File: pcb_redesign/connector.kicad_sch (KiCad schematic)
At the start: 8 parts, among them IC1 SPX1117M3-L-3-3_TR, J2 USB_B

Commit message: finished design
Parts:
- removed J2: USB_B, micro_usb_type_b:AMPHENOL_10118192-0002LF, symbol Connector:USB_B
- added J1: USB_B_Micro, micro_usb_type_b:AMPHENOL_10118192-0002LF, symbol Connector:USB_B_Micro
- C4: footprint 1uF_cap_0603:CL10A105KB8NNNC -> Capacitor_SMD:C_0603_1608Metric
- IC1: footprint SOT230P700X180-4N -> 3.3v_reg:SOT230P700X180-4N
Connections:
- net 3.7_UNREG: now also R3.1, J1.1 (VBUS)
- net D+: now also J1.3 (D+)
- net D-: now also J1.2 (D-)
- net GND: now also J1.5 (GND), J1.S1 (in1), J1.S2 (in2), J1.S3 (in3), J1.S4 (in4), J1.S5 (in5), J1.S6 (in6)
- net VCC_3V3: no longer R3.1
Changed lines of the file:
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@@
   (junction (at 177.8 35.56) (diameter 0) (color 0 0 0 0)
   )
+  (junction (at 35.56 95.25) (diameter 0) (color 0 0 0 0)
+  )
   (junction (at 177.8 54.61) (diameter 0) (color 0 0 0 0)
   )
@@
   (junction (at 57.15 54.61) (diameter 0) (color 0 0 0 0)
   )
+  (junction (at 35.56 100.33) (diameter 0) (color 0 0 0 0)
+  )
   (junction (at 232.41 55.88) (diameter 0) (color 0 0 0 0)
   )
+  (junction (at 35.56 102.87) (diameter 0) (color 0 0 0 0)
+  )
+  (junction (at 35.56 92.71) (diameter 0) (color 0 0 0 0)
+  )
+  (junction (at 57.15 80.01) (diameter 0) (color 0 0 0 0)
+  )
+  (junction (at 35.56 113.03) (diameter 0) (color 0 0 0 0)
+  )
   (junction (at 116.84 54.61) (diameter 0) (color 0 0 0 0)
   )
@@
   (junction (at 110.49 38.1) (diameter 0) (color 0 0 0 0)
   )
+  (junction (at 35.56 97.79) (diameter 0) (color 0 0 0 0)
+  )
   (junction (at 213.36 55.88) (diameter 0) (color 0 0 0 0)
   )
-  (no_connect (at 40.64 106.68))
-  (wire (pts (xy 78.74 80.01) (xy 80.01 80.01))
+  (no_connect (at 50.8 101.6))
+  (wire (pts (xy 57.15 80.01) (xy 80.01 80.01))
     (stroke (width 0) (type default))
   )
@@
     (stroke (width 0) (type default))
   )
+  (wire (pts (xy 35.56 102.87) (xy 35.56 113.03))
+    (stroke (width 0) (type default))
+  )
   (wire (pts (xy 50.8 99.06) (xy 142.24 99.06))
     (stroke (width 0) (type default))
@@
     (stroke (width 0) (type default))
   )
-  (wire (pts (xy 78.74 69.85) (xy 78.74 80.01))
-    (stroke (width 0) (type default))
-  )
   (wire (pts (xy 199.39 39.37) (xy 207.01 39.37))
     (stroke (width 0) (type default))
   )
-  (wire (pts (xy 57.15 91.44) (xy 57.15 54.61))
+  (wire (pts (xy 57.15 91.44) (xy 57.15 80.01))
     (stroke (width 0) (type default))
   )
@@
     (stroke (width 0) (type default))
   )
-  (wire (pts (xy 17.78 113.03) (xy 43.18 113.03))
+  (wire (pts (xy 17.78 113.03) (xy 35.56 113.03))
+    (stroke (width 0) (type default))
+  )
+  (wire (pts (xy 35.56 100.33) (xy 35.56 102.87))
     (stroke (width 0) (type default))
   )
@@
     (stroke (width 0) (type default))
   )
-  (wire (pts (xy 232.41 69.85) (xy 78.74 69.85))
-    (stroke (width 0) (type default))
-  )
   (wire (pts (xy 177.8 35.56) (xy 177.8 46.99))
     (stroke (width 0) (type default))
@@
     (stroke (width 0) (type default))
   )
+  (wire (pts (xy 35.56 113.03) (xy 43.18 113.03))
+    (stroke (width 0) (type default))
+  )
   (wire (pts (xy 182.88 46.99) (xy 177.8 46.99))
     (stroke (width 0) (type default))
@@
     (stroke (width 0) (type default))
   )
+  (wire (pts (xy 35.56 92.71) (xy 35.56 95.25))
+    (stroke (width 0) (type default))
+  )
   (wire (pts (xy 52.07 54.61) (xy 57.15 54.61))
     (stroke (width 0) (type default))
@@
     (stroke (width 0) (type default))
   )
+  (wire (pts (xy 57.15 80.01) (xy 57.15 54.61))
+    (stroke (width 0) (type default))
+  )
   (wire (pts (xy 116.84 41.91) (xy 116.84 38.1))
     (stroke (width 0) (type default))
@@
     (stroke (width 0) (type default))
   )
+  (wire (pts (xy 35.56 90.17) (xy 35.56 92.71))
+    (stroke (width 0) (type default))
+  )
   (wire (pts (xy 43.18 113.03) (xy 43.18 106.68))
     (stroke (width 0) (type default))
@@
     (stroke (width 0) (type default))
   )
+  (wire (pts (xy 35.56 95.25) (xy 35.56 97.79))
+    (stroke (width 0) (type default))
+  )
   (wire (pts (xy 50.8 91.44) (xy 57.15 91.44))
     (stroke (width 0) (type default))
@@
   )
   (wire (pts (xy 102.87 41.91) (xy 102.87 38.1))
+    (stroke (width 0) (type default))
+  )
+  (wire (pts (xy 35.56 97.79) (xy 35.56 100.33))
     (stroke (width 0) (type default))
   )
@@
       (effects (font (size 1.27 1.27)) (justify left))
     )
-    (property "Footprint" "1uF_cap_0603:CL10A105KB8NNNC" (at 102.87 48.26 0)
+    (property "Footprint" "Capacitor_SMD:C_0603_1608Metric" (at 102.87 48.26 0)
       (effects (font (size 1.27 1.27)) hide)
     )
@@
     )
   )
-  (symbol (lib_id "Connector:USB_B") (at 43.18 96.52 0) (unit 1)
-    (in_bom yes) (on_board yes) (dnp no) (fields_autoplaced)
-    (property "Reference" "J2" (at 43.18 85.09 0)
-      (effects (font (size 1.27 1.27)))
-    )
-    (property "Value" "USB_B" (at 43.18 87.63 0)
-      (effects (font (size 1.27 1.27)))
-    )
-    (property "Footprint" "micro_usb_type_b:AMPHENOL_10118192-0002LF" (at 46.99 97.79 0)
-      (effects (font (size 1.27 1.27)) hide)
-    )
-    (property "Datasheet" " ~" (at 46.99 97.79 0)
+  (symbol (lib_id "Connector:USB_B_Micro") (at 43.18 96.52 0) (unit 1)
+    (in_bom yes) (on_board yes) (dnp no) (fields_autoplaced)
+    (property "Reference" "J1" (at 43.18 85.09 0)
+      (effects (font (size 1.27 1.27)))
+    )
+    (property "Value" "USB_B_Micro" (at 43.18 87.63 0)
+      (effects (font (size 1.27 1.27)))
+    )
+    (property "Footprint" "micro_usb_type_b:AMPHENOL_10118192-0002LF" (at 48.26 106.68 0)
+      (effects (font (size 1.27 1.27)) hide)
+    )
+    (property "Datasheet" "~" (at 46.99 97.79 0)
       (effects (font (size 1.27 1.27)) hide)
     )
@@
     (pin "4")
     (pin "5")
-    (instances
-      (project "pcb_redesign"
-        (path "/fb030e39-7dd3-46a0-8379-c26b3ef1b0a0/2939bd35-2732-40e2-8b47-7f9c13890d54"
-          (reference "J2") (unit 1)
+    (pin "S5")
+    (pin "S6")
+    (pin "S1")
+    (pin "S2")
+    (pin "S3")
+    (pin "S4")
+    (instances
+      (project "pcb_redesign"
+        (path "/fb030e39-7dd3-46a0-8379-c26b3ef1b0a0/2939bd35-2732-40e2-8b47-7f9c13890d54"
+          (reference "J1") (unit 1)
         )
       )
@@
       (effects (font (size 1.27 1.27)))
     )
-    (property "Footprint" "SOT230P700X180-4N" (at 168.91 49.53 0)
+    (property "Footprint" "3.3v_reg:SOT230P700X180-4N" (at 168.91 49.53 0)
       (effects (font (size 1.27 1.27)) (justify left) hide)
     )

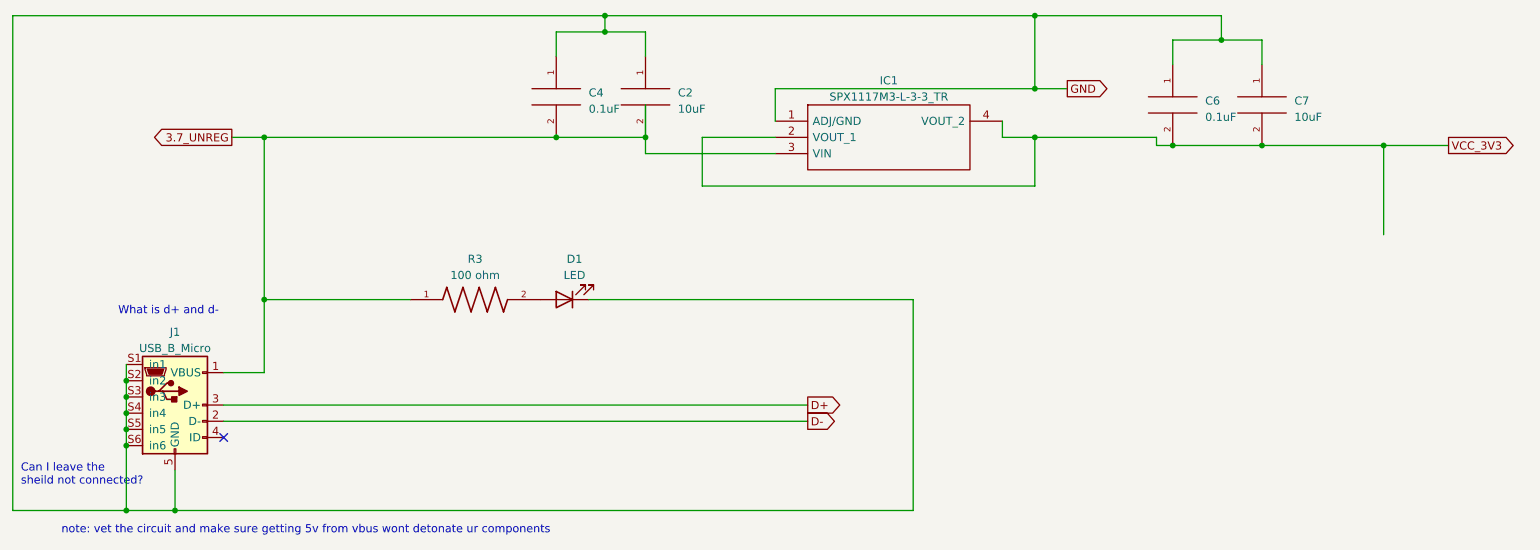
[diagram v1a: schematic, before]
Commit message: finished adding decoupling caps, shipped off to jlc
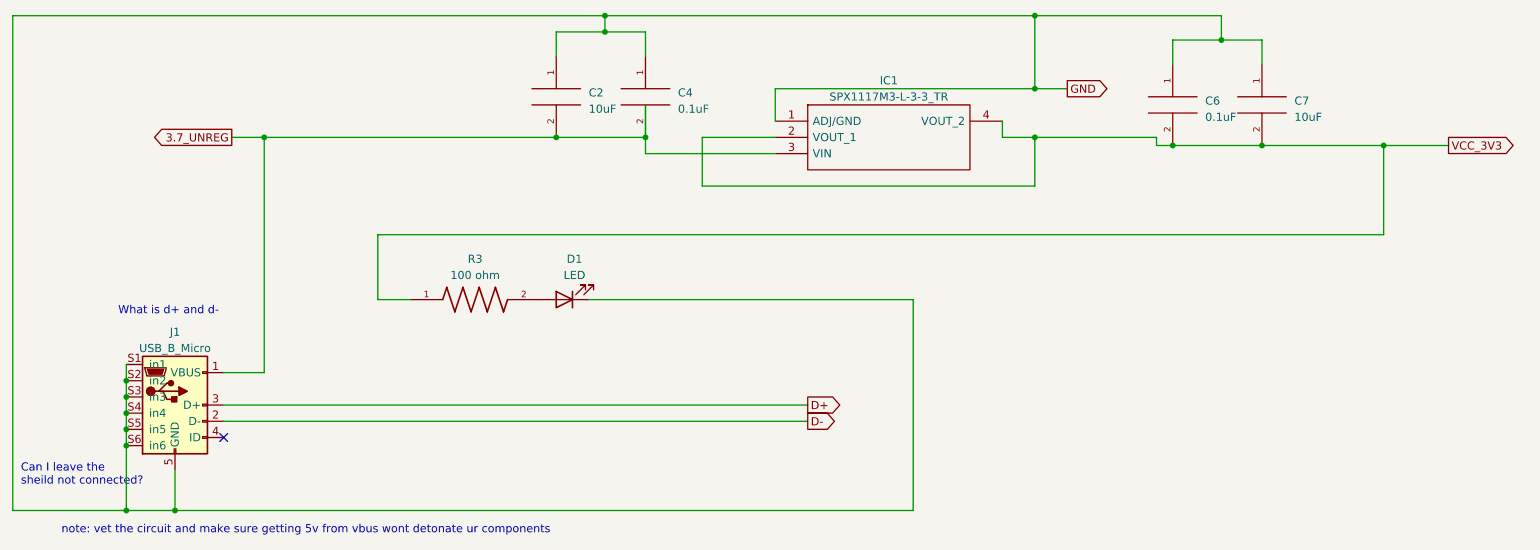
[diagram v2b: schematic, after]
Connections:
- net 3.7_UNREG: no longer R3.1
- net VCC_3V3: now also R3.1
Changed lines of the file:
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@@
 (kicad_sch (version 20230121) (generator eeschema)
   (paper "A4")
+  (junction (at 102.87 54.61) (diameter 0) (color 0 0 0 0)
+  )
   (junction (at 207.01 39.37) (diameter 0) (color 0 0 0 0)
   )
@@
   (junction (at 177.8 54.61) (diameter 0) (color 0 0 0 0)
   )
-  (junction (at 102.87 54.61) (diameter 0) (color 0 0 0 0)
-  )
   (junction (at 57.15 54.61) (diameter 0) (color 0 0 0 0)
   )
@@
   (junction (at 35.56 92.71) (diameter 0) (color 0 0 0 0)
   )
-  (junction (at 57.15 80.01) (diameter 0) (color 0 0 0 0)
-  )
   (junction (at 35.56 113.03) (diameter 0) (color 0 0 0 0)
   )
@@
   )
   (no_connect (at 50.8 101.6))
-  (wire (pts (xy 57.15 80.01) (xy 80.01 80.01))
-    (stroke (width 0) (type default))
-  )
   (wire (pts (xy 177.8 35.56) (xy 207.01 35.56))
     (stroke (width 0) (type default))
@@
     (stroke (width 0) (type default))
   )
+  (wire (pts (xy 74.93 80.01) (xy 74.93 69.85))
+    (stroke (width 0) (type default))
+  )
   (wire (pts (xy 199.39 43.18) (xy 199.39 39.37))
     (stroke (width 0) (type default))
@@
     (stroke (width 0) (type default))
   )
-  (wire (pts (xy 57.15 91.44) (xy 57.15 80.01))
-    (stroke (width 0) (type default))
-  )
   (wire (pts (xy 110.49 35.56) (xy 177.8 35.56))
     (stroke (width 0) (type default))
@@
     (stroke (width 0) (type default))
   )
+  (wire (pts (xy 74.93 69.85) (xy 232.41 69.85))
+    (stroke (width 0) (type default))
+  )
   (wire (pts (xy 35.56 100.33) (xy 35.56 102.87))
     (stroke (width 0) (type default))
   )
+  (wire (pts (xy 102.87 54.61) (xy 116.84 54.61))
+    (stroke (width 0) (type default))
+  )
   (wire (pts (xy 110.49 38.1) (xy 116.84 38.1))
     (stroke (width 0) (type default))
@@
     (stroke (width 0) (type default))
   )
-  (wire (pts (xy 57.15 80.01) (xy 57.15 54.61))
+  (wire (pts (xy 80.01 80.01) (xy 74.93 80.01))
+    (stroke (width 0) (type default))
+  )
+  (wire (pts (xy 57.15 54.61) (xy 57.15 91.44))
     (stroke (width 0) (type default))
   )
@@
   )
   (wire (pts (xy 196.85 55.88) (xy 199.39 55.88))
-    (stroke (width 0) (type default))
-  )
-  (wire (pts (xy 102.87 54.61) (xy 116.84 54.61))
     (stroke (width 0) (type default))
   )
@@
     )
   )
-  (symbol (lib_id "pspice:C") (at 102.87 48.26 0) (unit 1)
-    (in_bom yes) (on_board yes) (dnp no) (fields_autoplaced)
-    (property "Reference" "C4" (at 107.95 47.625 0)
-      (effects (font (size 1.27 1.27)) (justify left))
-    )
-    (property "Value" "0.1uF" (at 107.95 50.165 0)
-      (effects (font (size 1.27 1.27)) (justify left))
-    )
-    (property "Footprint" "Capacitor_SMD:C_0603_1608Metric" (at 102.87 48.26 0)
-      (effects (font (size 1.27 1.27)) hide)
-    )
-    (property "Datasheet" "~" (at 102.87 48.26 0)
-      (effects (font (size 1.27 1.27)) hide)
-    )
-    (pin "1")
-    (pin "2")
-    (instances
-      (project "pcb_redesign"
-        (path "/fb030e39-7dd3-46a0-8379-c26b3ef1b0a0/2939bd35-2732-40e2-8b47-7f9c13890d54"
-          (reference "C4") (unit 1)
-        )
-      )
-    )
-  )
   (symbol (lib_id "pspice:C") (at 213.36 49.53 0) (unit 1)
     (in_bom yes) (on_board yes) (dnp no) (fields_autoplaced)
@@
         (path "/fb030e39-7dd3-46a0-8379-c26b3ef1b0a0/2939bd35-2732-40e2-8b47-7f9c13890d54"
           (reference "C7") (unit 1)
-        )
-      )
-    )
-  )
-  (symbol (lib_id "pspice:C") (at 116.84 48.26 0) (unit 1)
-    (in_bom yes) (on_board yes) (dnp no) (fields_autoplaced)
-    (property "Reference" "C2" (at 121.92 47.625 0)
-      (effects (font (size 1.27 1.27)) (justify left))
-    )
-    (property "Value" "10uF" (at 121.92 50.165 0)
-      (effects (font (size 1.27 1.27)) (justify left))
-    )
-    (property "Footprint" "10uF_cap_0603:CAPC1608X90N" (at 116.84 48.26 0)
-      (effects (font (size 1.27 1.27)) hide)
-    )
-    (property "Datasheet" "~" (at 116.84 48.26 0)
-      (effects (font (size 1.27 1.27)) hide)
-    )
-    (pin "1")
-    (pin "2")
-    (instances
-      (project "pcb_redesign"
-        (path "/fb030e39-7dd3-46a0-8379-c26b3ef1b0a0/2939bd35-2732-40e2-8b47-7f9c13890d54"
-          (reference "C2") (unit 1)
         )
       )
@@
     (pin "4")
     (pin "5")
-    (pin "S5")
-    (pin "S6")
     (pin "S1")
     (pin "S2")
     (pin "S3")
     (pin "S4")
+    (pin "S5")
+    (pin "S6")
     (instances
       (project "pcb_redesign"
@@
         )
       )
+    )
+  )
+  (symbol (lib_id "pspice:C") (at 102.87 48.26 0) (unit 1)
+    (in_bom yes) (on_board yes) (dnp no) (fields_autoplaced)
+    (property "Reference" "C2" (at 107.95 47.625 0)
+      (effects (font (size 1.27 1.27)) (justify left))
+    )
+    (property "Value" "10uF" (at 107.95 50.165 0)
+      (effects (font (size 1.27 1.27)) (justify left))
+    )
+    (property "Footprint" "10uF_cap_0603:CAPC1608X90N" (at 102.87 48.26 0)
+      (effects (font (size 1.27 1.27)) hide)
+    )
+    (property "Datasheet" "~" (at 102.87 48.26 0)
+      (effects (font (size 1.27 1.27)) hide)
+    )
+    (pin "1")
+    (pin "2")
+    (instances
+      (project "pcb_redesign"
+        (path "/fb030e39-7dd3-46a0-8379-c26b3ef1b0a0/2939bd35-2732-40e2-8b47-7f9c13890d54"
+          (reference "C2") (unit 1)
+        )
+      )
+    )
+  )
+  (symbol (lib_id "pspice:C") (at 116.84 48.26 0) (unit 1)
+    (in_bom yes) (on_board yes) (dnp no) (fields_autoplaced)
+    (property "Reference" "C4" (at 121.92 47.625 0)
+      (effects (font (size 1.27 1.27)) (justify left))
+    )
+    (property "Value" "0.1uF" (at 121.92 50.165 0)
+      (effects (font (size 1.27 1.27)) (justify left))
+    )
+    (property "Footprint" "Capacitor_SMD:C_0603_1608Metric" (at 116.84 48.26 0)
+      (effects (font (size 1.27 1.27)) hide)
+    )
+    (property "Datasheet" "~" (at 116.84 48.26 0)
+      (effects (font (size 1.27 1.27)) hide)
+    )
+    (pin "1")
+    (pin "2")
+    (instances
+      (project "pcb_redesign"
+        (path "/fb030e39-7dd3-46a0-8379-c26b3ef1b0a0/2939bd35-2732-40e2-8b47-7f9c13890d54"
+          (reference "C4") (unit 1)
+        )
+      )
